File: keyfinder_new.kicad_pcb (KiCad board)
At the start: 2 copper layers, 20 x 14 mm, 20 parts, among them U1 NRF52832, X1 32MHz, X2 32.768kHz

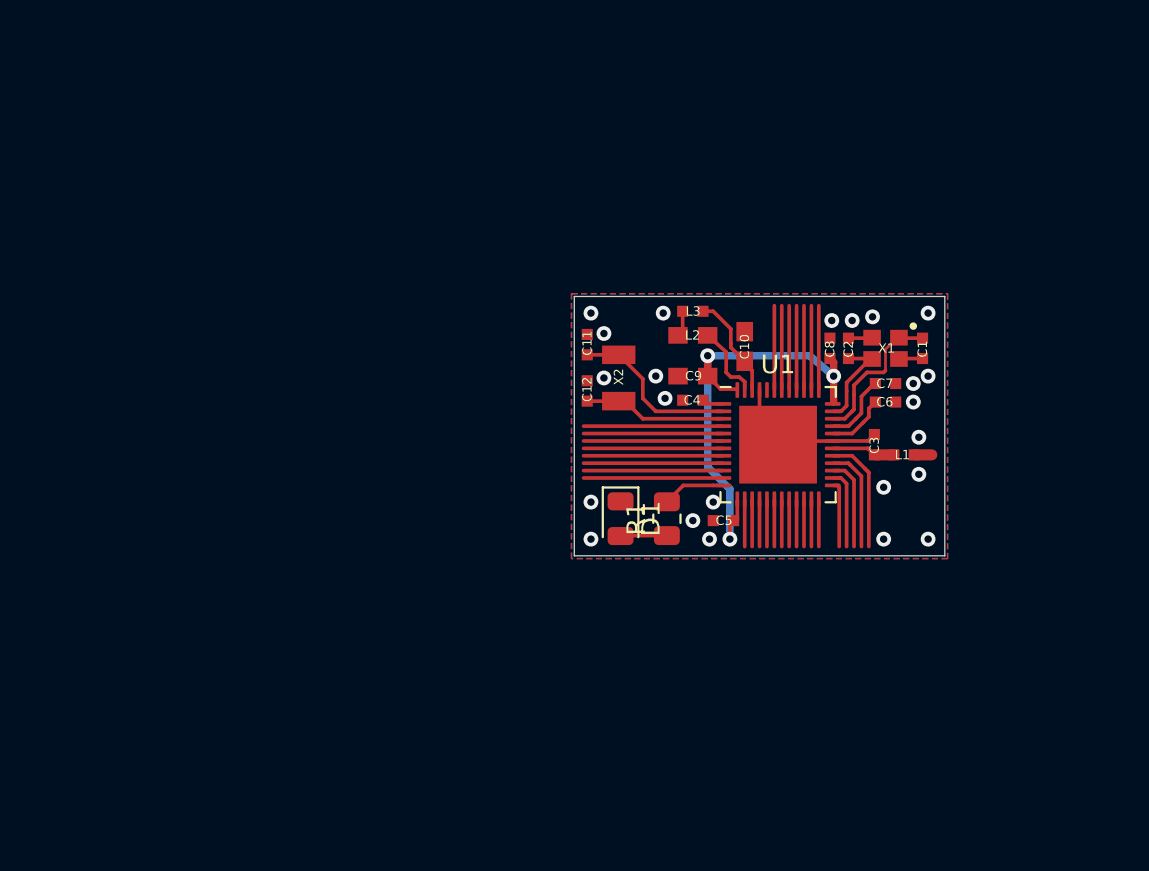
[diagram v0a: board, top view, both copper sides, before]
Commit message: Ajout de quelques composants sur le schema
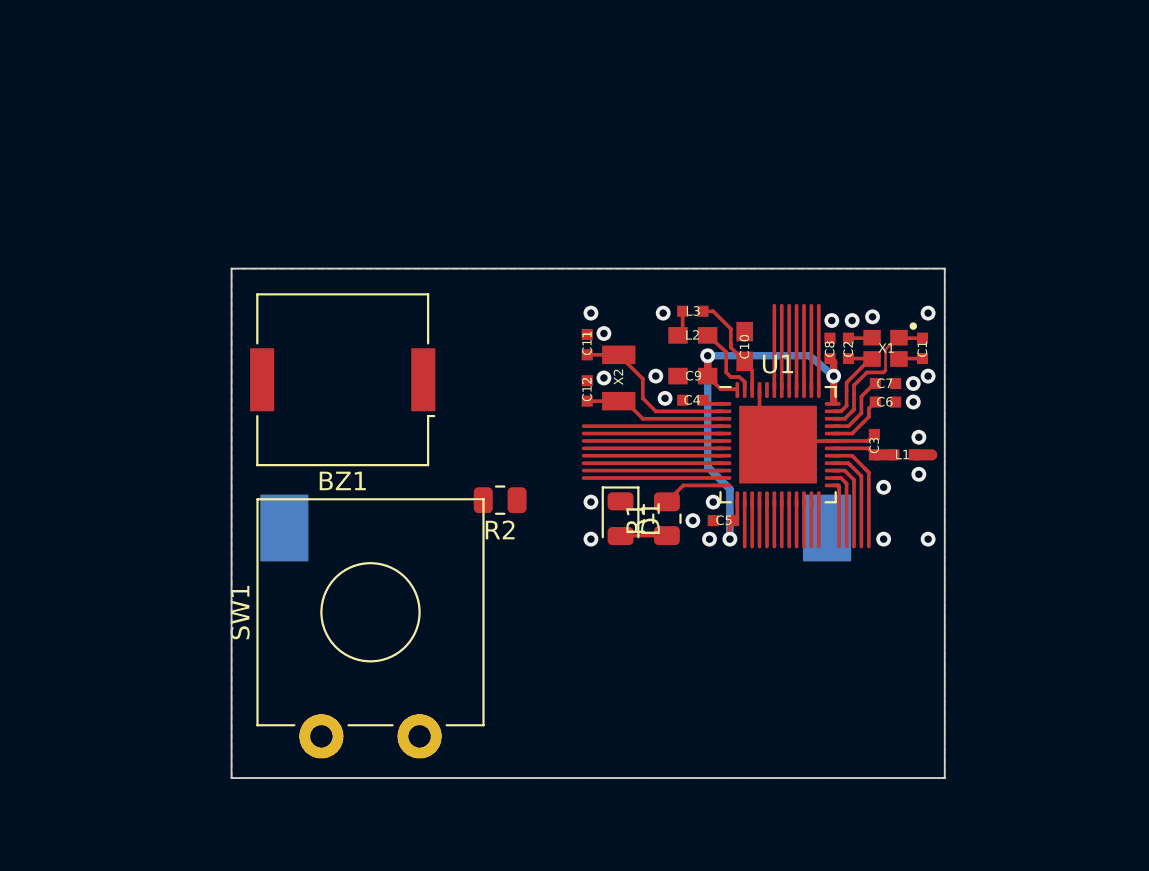
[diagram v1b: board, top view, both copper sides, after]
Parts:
- added BT1: Battery, Battery:BatteryHolder_Keystone_1060_1x2032, B.Cu at (137.5, 110.5)
- added BZ1: Buzzer, Buzzer_Beeper:Buzzer_Murata_PKMCS0909E, F.Cu at (126.0, 102.5)
- added R2: 10k, Resistor_SMD:R_0805_2012Metric, F.Cu at (134.5, 109.0)
- added SW1: SW_Push, Button_Switch_THT:SW_CW_GPTS203211B, F.Cu at (124.8, 121.8)
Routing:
- net VCC: vias 0 -> 1
- net GND: vias 23 -> 22
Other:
- board size 20 x 14 mm -> 38.5 x 27.5 mm

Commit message: Ajout des composants manquants et debut du routage sur le PCB
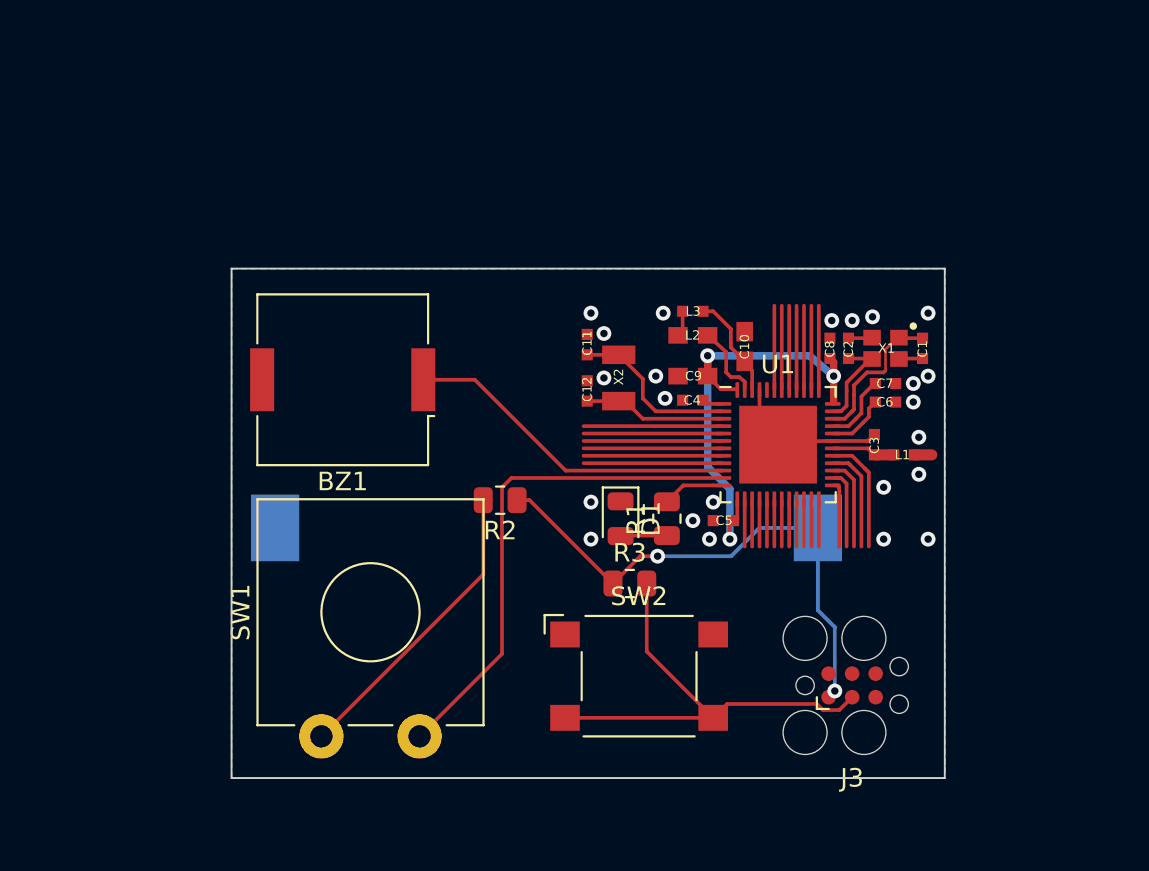
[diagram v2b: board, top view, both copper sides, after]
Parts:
- added J3: Conn_ARM_SWD_TagConnect_TC2030, Connector:Tag-Connect_TC2030-IDC-FP_2x03_P1.27mm_Vertical, F.Cu at (153.5, 119.0)
- added R3: 10k, Resistor_SMD:R_0805_2012Metric, F.Cu at (141.5, 113.5)
- added SW2: SW_Omron_B3FS, Button_Switch_SMD:SW_SPST_Omron_B3FS-100xP, F.Cu at (142.0, 118.5)
- moved BT1 0.50 mm to (137.0, 110.5)
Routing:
- net VCC: track 0.00 -> 29.0 mm, vias 1 -> 4
- net /P0.21/RESET: track 2.50 -> 27.5 mm
- net /P0.09: track 7.50 -> 27.4 mm
- net Net-(R2-Pad2): track 0.00 -> 16.4 mm
- net /P0.08: track 7.50 -> 18.2 mm
- net GND: vias 22 -> 21

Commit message: Fin du routage
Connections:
- BT1 pad 1: VCC -> VDD_P3V3
- J3 pad 1: VCC -> VDD_P3V3
- R2 pad 1: VCC -> VDD_P3V3
- R3 pad 1: VCC -> VDD_P3V3
- U1 pad 13: VCC -> VDD_P3V3
- U1 pad 36: VCC -> VDD_P3V3
- U1 pad 48: VCC -> VDD_P3V3
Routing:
- net VDD_P3V3: track 25.6 -> 55.7 mm, vias 3 -> 6
- net VCC: track 29.0 -> 0.00 mm, vias 4 -> 0
- net /P0.21/RESET: track 27.5 -> 39.1 mm
- net /SWDCLK: track 3.54 -> 14.6 mm, vias 0 -> 2
- net /SWDIO: track 4.22 -> 11.7 mm

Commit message: Correction des problemes de VCC et ajout dimensions
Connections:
- net VDD_P3V3 renamed VCC

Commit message: Passage sur le vrai PCB
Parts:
- J3: footprint Connector:Tag-Connect_TC2030-IDC-FP_2x03_P1.27mm_Vertical -> Connector:Tag-Connect_TC2030-IDC-NL_2x03_P1.27mm_Vertical
- R1: value 75 -> 330
- SW1: footprint Button_Switch_THT:SW_CW_GPTS203211B -> Button_Switch_SMD:SW_SPST_PTS810
- SW2: footprint Button_Switch_SMD:SW_SPST_Omron_B3FS-100xP -> Button_Switch_SMD:SW_SPST_PTS810
- moved SW1 20.8 mm to (139.0, 106.5), turned to 180 degrees
- moved D1 18.3 mm to (159.0, 106.5)
- moved R2 7.43 mm to (137.0, 102.0), turned to -90 degrees
- moved SW2 7.39 mm to (148.9, 115.9)
- moved J3 6.43 mm to (158.0, 114.4)
- moved BZ1 4.61 mm to (130.5, 103.5)
- moved BT1 3.81 mm to (138.5, 107.0)
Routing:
- net Net-(D1-A): track 2.51 -> 30.1 mm, vias 0 -> 2
- net /P0.09: track 27.4 -> 10.6 mm
- net /P0.21/RESET: track 39.1 -> 25.0 mm
- net VCC: track 55.7 -> 64.2 mm
- net /P0.07: track 7.50 -> 0.00 mm
- net /P0.06: track 7.50 -> 0.00 mm
- net /P0.05: track 7.50 -> 0.00 mm
- net /P0.04: track 7.50 -> 0.00 mm
- net /P0.03: track 7.50 -> 0.00 mm
- net /P0.02: track 7.50 -> 0.00 mm
- net /P0.24: track 6.27 -> 0.00 mm
- net /P0.23: track 5.59 -> 0.00 mm
- net /P0.22: track 4.91 -> 0.00 mm
- net /P0.08: track 18.2 -> 13.3 mm
- net /SWDCLK: track 14.6 -> 11.1 mm
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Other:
- board size 38.5 x 27.5 mm -> 40.7 x 32 mm

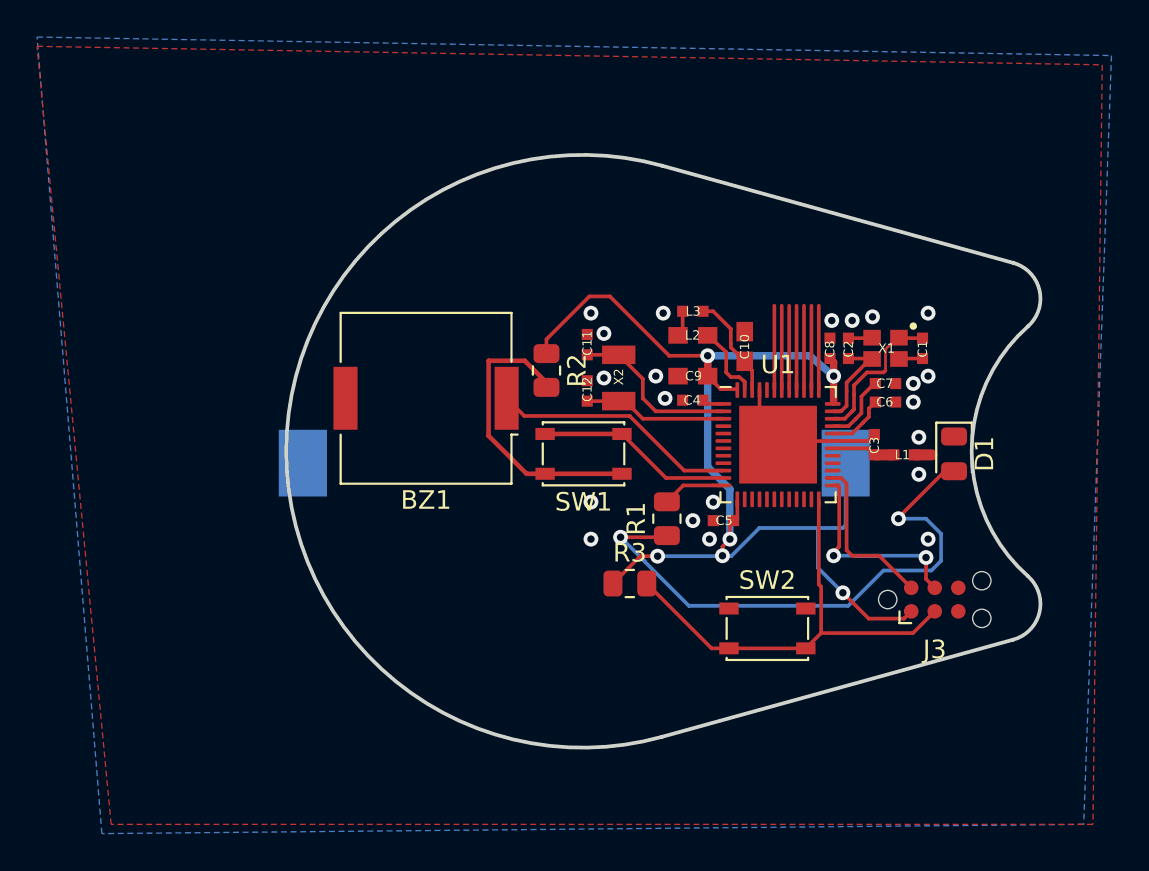
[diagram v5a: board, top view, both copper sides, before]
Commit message: Ajout du capteur de temperature au schema et au PCB et routage
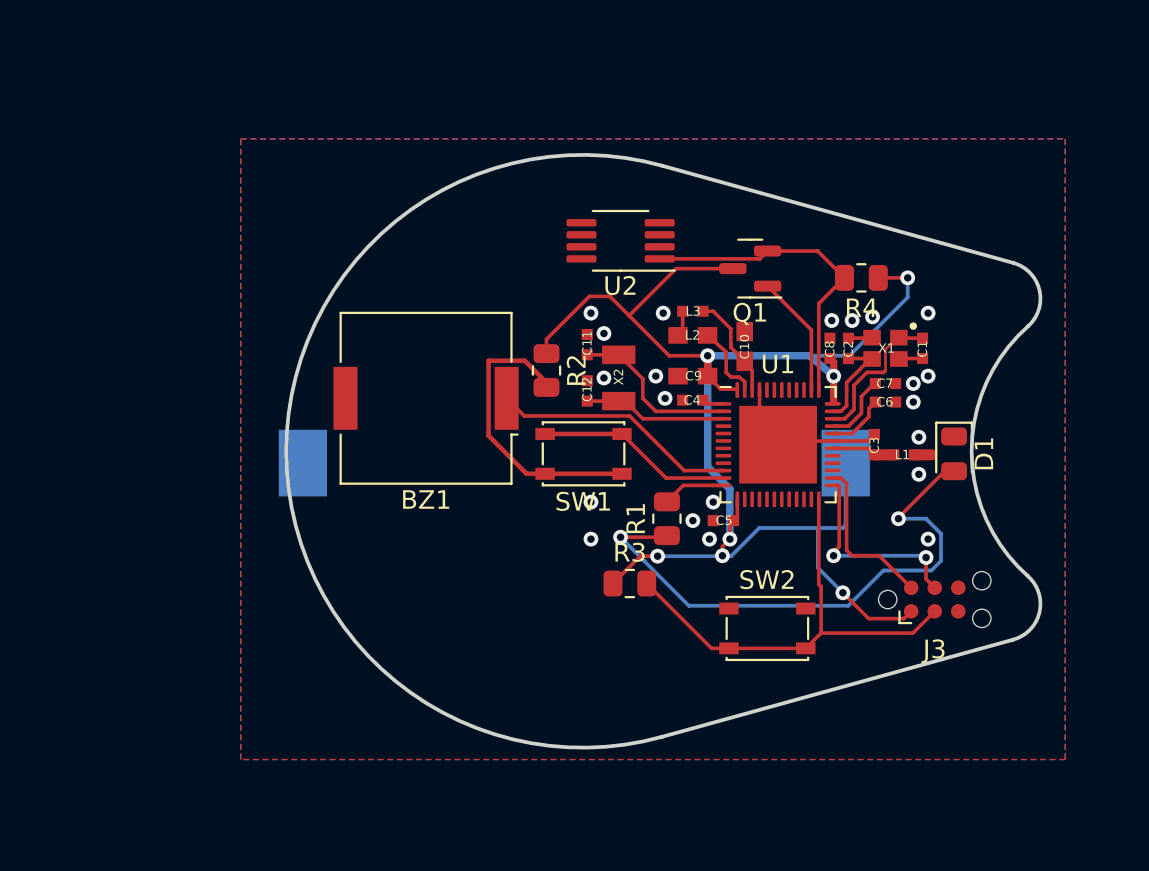
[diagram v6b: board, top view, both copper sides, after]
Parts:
- added Q1: 2N7002, Package_TO_SOT_SMD:SOT-23, F.Cu at (148.0, 96.5)
- added R4: 4.7k, Resistor_SMD:R_0805_2012Metric, F.Cu at (154.0, 97.0)
- added U2: DS18B20U, Package_SO:MSOP-8_3x3mm_P0.65mm, F.Cu at (141.0, 95.0)
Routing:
- net VCC: track 64.2 -> 80.0 mm, vias 6 -> 7
- net /P0.25: track 4.50 -> 17.4 mm
- net /P0.31: track 4.50 -> 0.00 mm
- net /P0.30: track 4.50 -> 0.00 mm
- net /P0.29: track 4.50 -> 0.00 mm
- net /P0.28: track 4.50 -> 0.00 mm
- net /P0.27: track 4.50 -> 0.00 mm
- net /P0.26: track 4.50 -> 6.58 mm
